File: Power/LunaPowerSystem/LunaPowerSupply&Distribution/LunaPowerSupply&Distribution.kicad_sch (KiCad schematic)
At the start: 2 parts

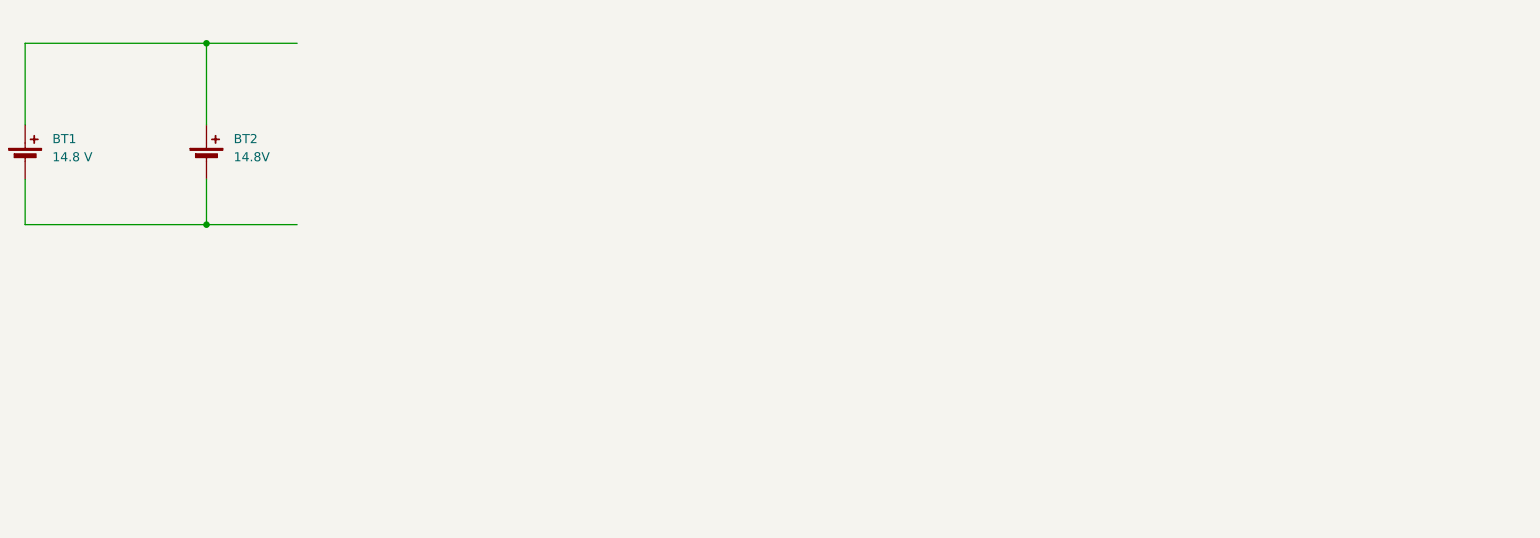
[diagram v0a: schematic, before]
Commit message: Fixed things
At least my version of the mech schematic was broken, so I copied in the last version committed by Alex, and I updated the power schematic to use library symbols
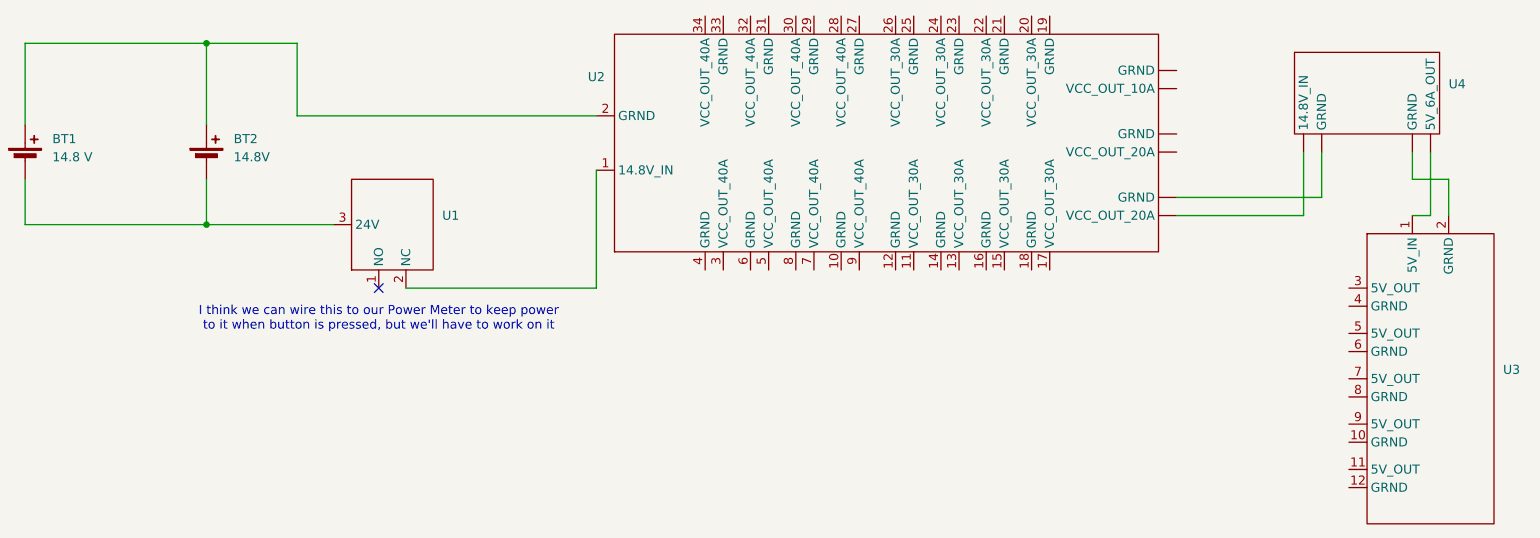
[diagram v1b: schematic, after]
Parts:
- added U1: ~, symbol Lunabotics 2025-26:A22E-M-11
- added U2: ~, symbol Lunabotics 2025-26:Power_Distribution_Panel
- added U3: ~, symbol Lunabotics 2025-26:Mini_Power_Distribution_Panel
- added U4: ~, symbol Lunabotics 2025-26:Volt._Reg._14.8-5V
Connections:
- net at BT1.1 (+), BT2.1 (+): now also U2.2 (GRND)
- net at BT1.2 (-), BT2.2 (-): now also U1.3 (24V)
- new net: U2. (GRND), U4. (5V_6A_OUT) (x2)
- new net: U1.2 (NC), U2.1 (14.8V_IN)
- new net: U3.1 (5V_IN), U4. (5V_6A_OUT)
- new net: U3.2 (GRND), U4. (5V_6A_OUT)
- no-connect marks 0 -> 1
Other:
- note added: "I think we can wire this to our Power Meter to keep power to it when button is pressed, but we'll have to work on it"

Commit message: Updated Power System Schematic
Updated Power System Schematic with power meter and E-stop. Added power meter symbol and modified existing E-Stop symbol.
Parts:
- added U5: ~, symbol Lunabotics 2025-26:Power_Meter
- added U6: ~, symbol Lunabotics 2025-26:Jetson_Nano
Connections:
- net at BT1.1 (+), BT2.1 (+): now also U5.2 (S-); no longer U2.2 (GRND)
- net at BT1.2 (-), BT2.2 (-): now also U5.1 (S+); no longer U1.3 (24V)
- net at U2. (GRND): now also U4. (5V_6A_OUT)
- net at U4. (5V_6A_OUT): now also U3.2 (GRND); no longer U2. (GRND)
- net at U1.1 (NO): now also U2.2 (GRND), U5.4 (L-)
- new net: U2. (GRND), U4. (5V_6A_OUT)
- new net: U1.3 (14.8V), U5.3 (L+)
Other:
- note removed: "I think we can wire this to our Power Meter to keep power to it when button is pressed, but we'll have to work on it"
- moved on the sheet: BT1, BT2, U3

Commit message: Updated Power Supply System
Added Motor Controllers, Jetson Nano,  and IMU.
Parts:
- added C1, C2: C, symbol Device:C
- added U10, U7, U8, U9: ~, symbol Lunabotics 2025-26:Spark_MAX_Motor_Controller
- added U11: MPU-6050, Sensor_Motion:InvenSense_QFN-24_4x4mm_P0.5mm, symbol Sensor_Motion:MPU-6050
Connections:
- net at U6.17 ((J7)_GND_1): now also U3.3 (5V_OUT)
- net at U6.18 ((J7)_PWR_(5V)_2): now also U3.4 (GRND)
- net at U6.21 ((J6)_3.3_VDC_1): now also U11.13 (VDD), U11.8 (VLOGIC)
- net at U2. (GRND): now also U4. (5V_6A_OUT)
- net at U4. (5V_6A_OUT): now also U3.2 (GRND); no longer U2. (GRND)
- net at U2.3 (VCC_OUT_40A): now also U7.4 (V+)
- net at U2.31 (GRND): now also U10.5 (V-)
- net at U2.32 (VCC_OUT_40A): now also U10.4 (V+)
- net at U2.33 (GRND): now also U9.5 (V-)
- net at U2.34 (VCC_OUT_40A): now also U9.4 (V+)
- net at U2.4 (GRND): now also U7.5 (V-)
- net at U2.5 (VCC_OUT_40A): now also U8.4 (V+)
- net at U2.6 (GRND): now also U8.5 (V-)
- new net: U2. (GRND), U4. (5V_6A_OUT)
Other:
- moved on the sheet: BT1, BT2, U1, U2, U3, U4, U5
